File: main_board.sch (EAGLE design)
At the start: 49 parts, among them IC1 LT1168ACS8, IC2 LT1168ACS8, IC3 LT1168ACS8, IC4 317EMP, U1 TLC272IP, U2 TLC272IP, U3 TLC272IP

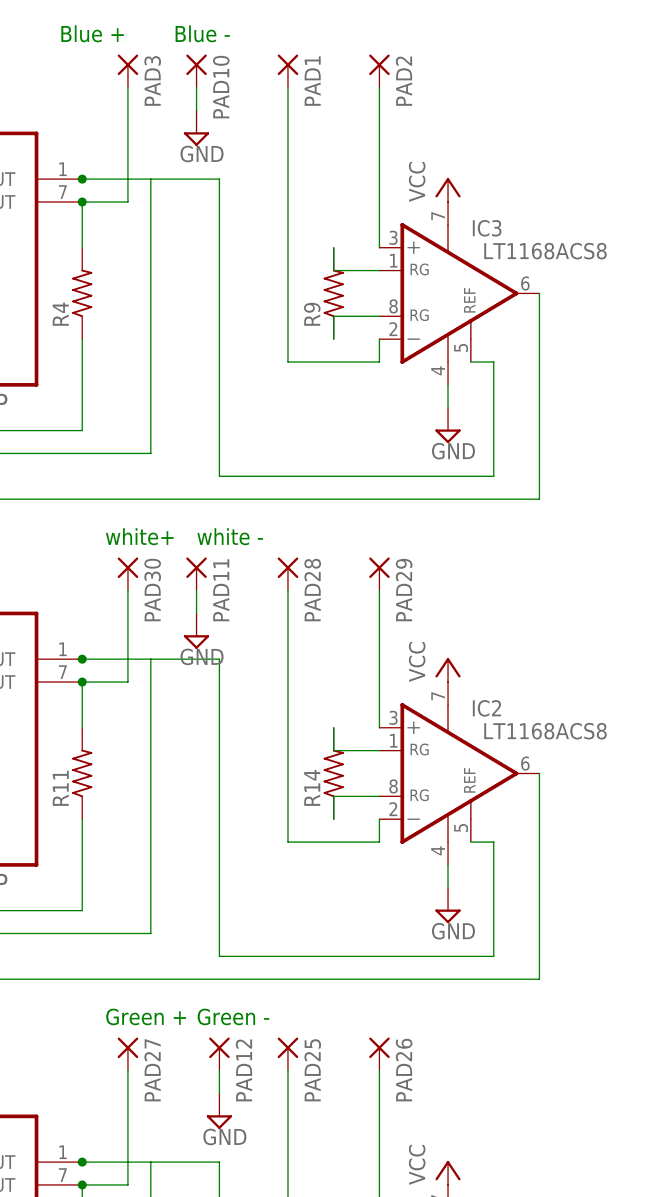
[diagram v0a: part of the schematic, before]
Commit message: Added bill of materials
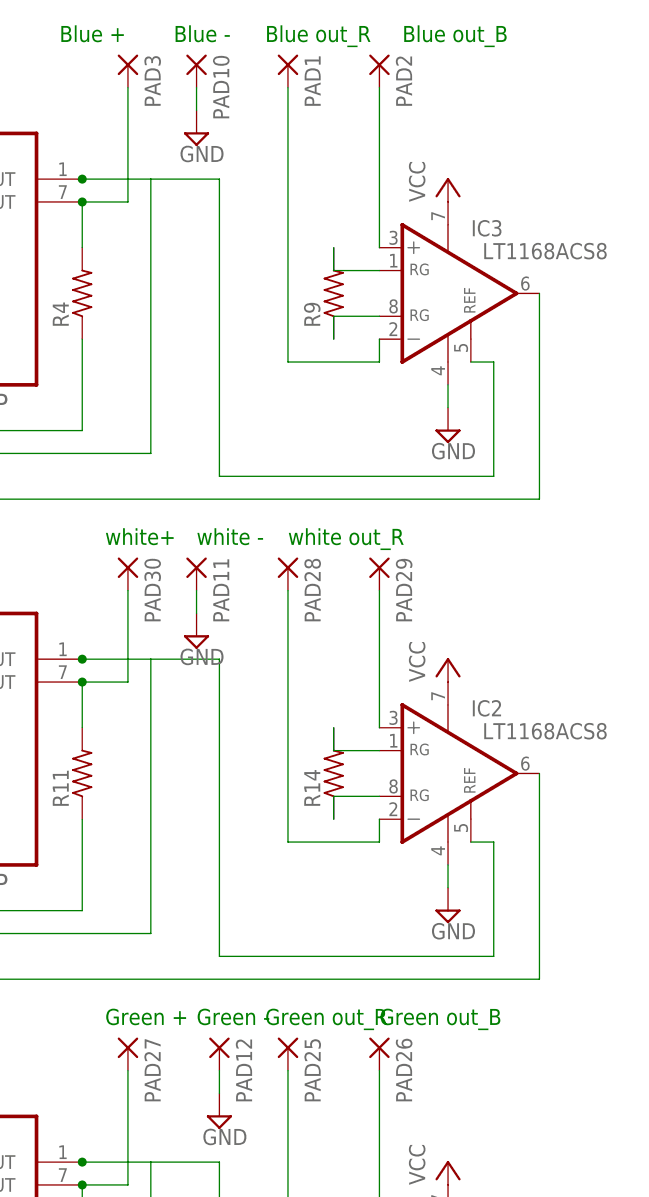
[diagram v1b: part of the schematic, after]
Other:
- note added: "Blue out_B"
- note added: "Blue out_R"
- note added: "Green out_B"
- note added: "Green out_R"
- note added: "white out_R"
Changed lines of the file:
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@@
 <?xml version="1.0" encoding="utf-8"?>
 <!DOCTYPE eagle SYSTEM "eagle.dtd">
-<eagle version="8.2.2">
+<eagle version="8.2.1">
 <drawing>
 <settings>
@@
 <text x="154.94" y="58.42" size="1.778" layer="91">Green - </text>
 <text x="38.1" y="68.58" size="1.778" layer="91">white-</text>
+<text x="165.1" y="111.76" size="1.778" layer="91">white out_R</text>
+<text x="175.26" y="58.42" size="1.778" layer="91">Green out_B</text>
+<text x="162.56" y="58.42" size="1.778" layer="91">Green out_R</text>
+<text x="162.56" y="167.64" size="1.778" layer="91">Blue out_R</text>
+<text x="177.8" y="167.64" size="1.778" layer="91">Blue out_B</text>
 </plain>
 <instances>
